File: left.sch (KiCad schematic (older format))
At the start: 87 parts, among them J1 Buzzer_magnetic, J11 Conn_01x01, J12 Conn_01x01, J13 Conn_01x01, J14 Conn_01x01, J15 Conn_01x01, J16 Conn_01x01, J17 Conn_01x01, J2 reset, J25 Buzzer_piezo, J3 ISP, J7 Conn_01x01, J9 UTC16-G, P3 WS2812, P4 SJ-43514-SMT, SW1 Socket, SW10 Socket, SW11 Socket, SW12 Socket, SW13 Socket, SW14 Socket, SW15 Socket, SW16 Socket, SW17 Socket, SW18 Socket, SW19 Socket, SW2 Socket, SW20 Socket, SW21 Socket, SW22 Socket, SW23 Socket, SW24 Socket, SW3 Socket, SW4 Socket, SW49 FSMSM, SW5 Socket, SW6 Socket, SW7 Socket, SW8 Socket, SW9 Socket, U1 ATMega32U4, Y1 16MHz

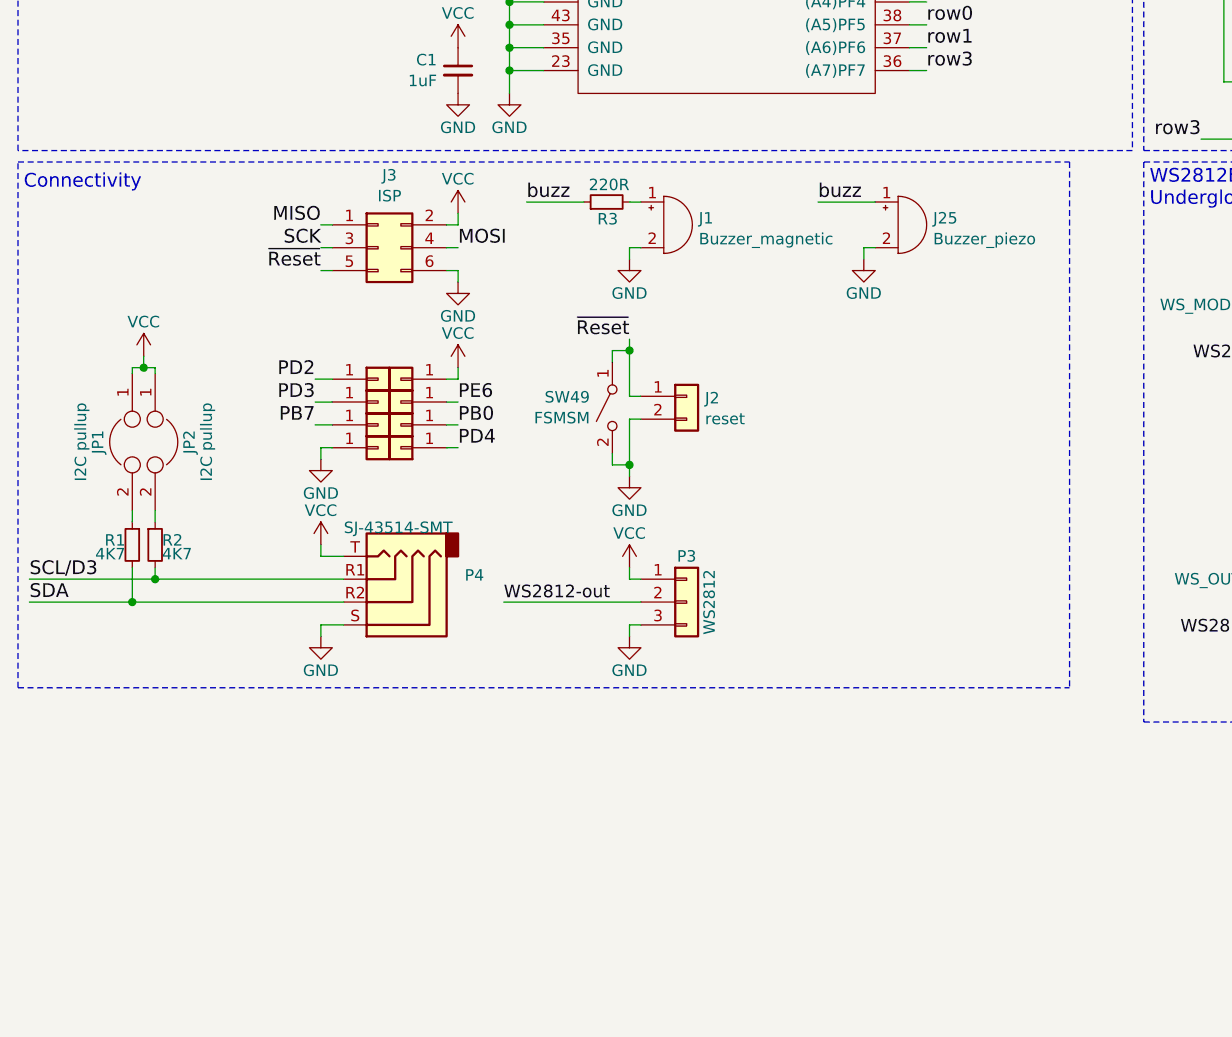
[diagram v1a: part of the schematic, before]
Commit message: Added ESD protection to connectors
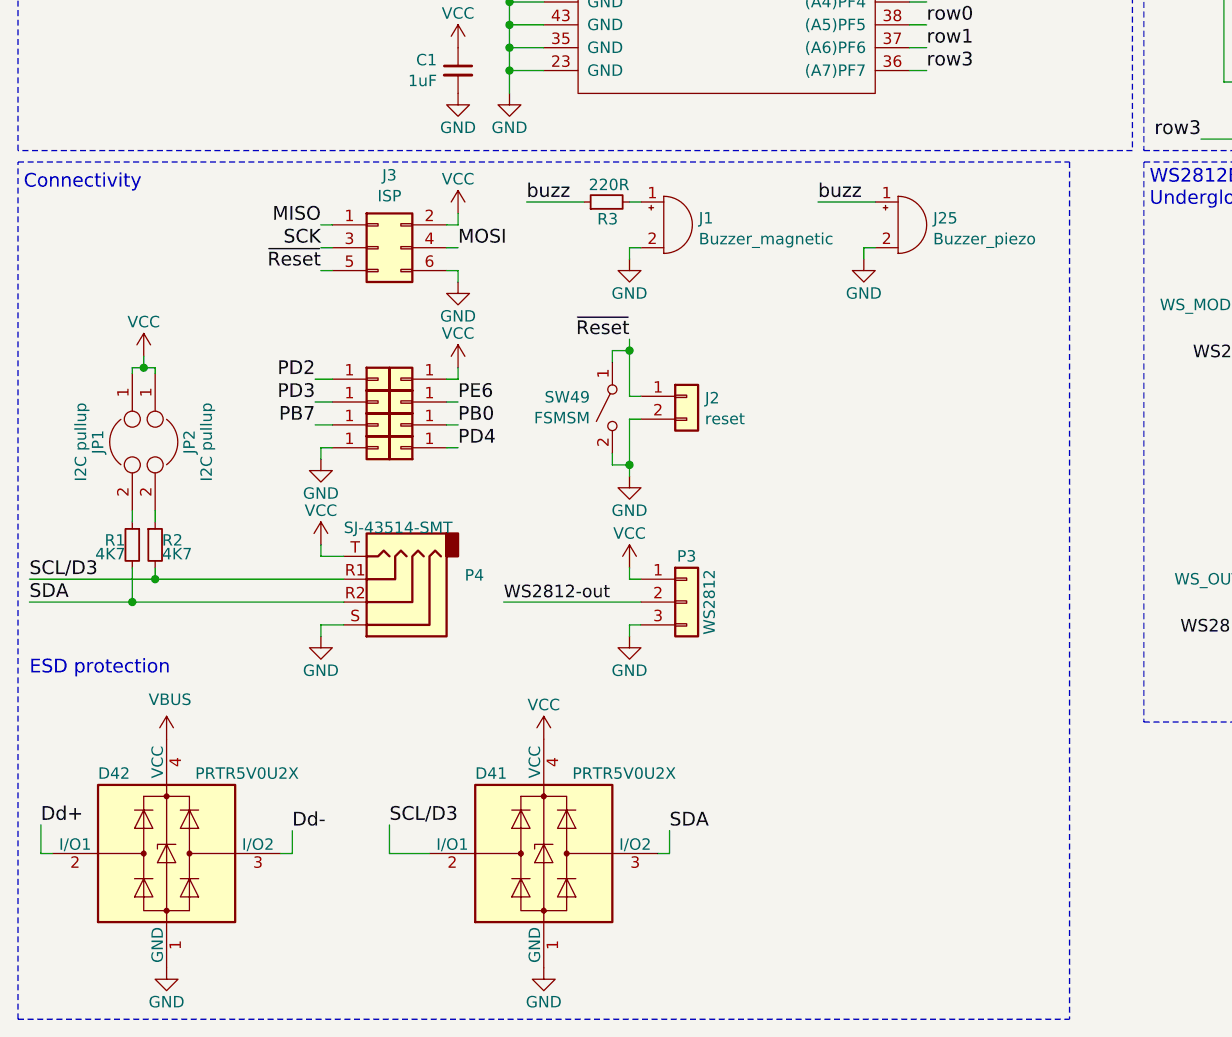
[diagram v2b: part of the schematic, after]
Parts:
- added D41, D42: PRTR5V0U2X, Package_TO_SOT_SMD:SOT-143, symbol Power_Protection:PRTR5V0U2X
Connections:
- net Dd+: now also D42.2 (I/O1)
- net Dd-: now also D42.3 (I/O2)
- net GND: now also D41.1 (GND), D42.1 (GND)
- net SCL/D3: now also D41.2 (I/O1)
- net SDA: now also D41.3 (I/O2)
- net VBUS: now also D42.4 (VCC)
- net VCC: now also D41.4 (VCC)
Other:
- note added: "ESD protection"
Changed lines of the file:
@@
 	875  5925 1325 5925
 Wire Notes Line
-	825  6300 825  4000
+	825  7750 825  4000
 Wire Notes Line
 	825  4000 5425 4000
 Wire Notes Line
-	5425 4000 5425 6300
+	5425 4000 5425 7750
 Wire Notes Line
-	825  6300 5425 6300
+	825  7750 5425 7750
 Text Notes 850  4125 0    60   ~ 0
 Connectivity
@@
 Wire Wire Line
 	4725 2850 4800 2850
+$Comp
+L Power_Protection:PRTR5V0U2X D42
+U 1 1 5D9D619E
+P 1475 7025
+F 0 "D42" H 1175 7375 50  0000 L CNN
+F 1 "PRTR5V0U2X" H 1600 7375 50  0000 L CNN
+F 2 "Package_TO_SOT_SMD:SOT-143" H 1535 7025 50  0001 C CNN
+F 3 "https://assets.nexperia.com/documents/data-sheet/PRTR5V0U2X.pdf" H 1535 7025 50  0001 C CNN
+	1    1475 7025
+	1    0    0    -1
+$EndComp
+$Comp
+L power:VBUS #PWR0131
+U 1 1 5DA6A0DF
+P 1475 6525
+F 0 "#PWR0131" H 1475 6375 50  0001 C CNN
+F 1 "VBUS" H 1490 6698 50  0000 C CNN
+F 2 "" H 1475 6525 50  0001 C CNN
+F 3 "" H 1475 6525 50  0001 C CNN
+	1    1475 6525
+	1    0    0    -1
+$EndComp
+$Comp
+L power:GND #PWR0132
+U 1 1 5DA6AF0C
+P 1475 7525
+F 0 "#PWR0132" H 1475 7275 50  0001 C CNN
+F 1 "GND" H 1475 7375 50  0000 C CNN
+F 2 "" H 1475 7525 50  0000 C CNN
+F 3 "" H 1475 7525 50  0000 C CNN
+	1    1475 7525
+	-1   0    0    -1
+$EndComp
+Wire Wire Line
+	975  7025 925  7025
+Wire Wire Line
+	925  7025 925  6900
+Wire Wire Line
+	1975 7025 2025 7025
+Wire Wire Line
+	2025 7025 2025 6925
+Text Label 925  6900 0    60   ~ 0
+Dd+
+Text Label 2025 6925 0    60   ~ 0
+Dd-
+Text Notes 875  6250 0    60   ~ 0
+ESD protection
+$Comp
+L Power_Protection:PRTR5V0U2X D41
+U 1 1 5DDB696C
+P 3125 7025
+F 0 "D41" H 2825 7375 50  0000 L CNN
+F 1 "PRTR5V0U2X" H 3250 7375 50  0000 L CNN
+F 2 "Package_TO_SOT_SMD:SOT-143" H 3185 7025 50  0001 C CNN
+F 3 "https://assets.nexperia.com/documents/data-sheet/PRTR5V0U2X.pdf" H 3185 7025 50  0001 C CNN
+	1    3125 7025
+	1    0    0    -1
+$EndComp
+$Comp
+L power:GND #PWR0136
+U 1 1 5DDB6980
+P 3125 7525
+F 0 "#PWR0136" H 3125 7275 50  0001 C CNN
+F 1 "GND" H 3125 7375 50  0000 C CNN
+F 2 "" H 3125 7525 50  0000 C CNN
+F 3 "" H 3125 7525 50  0000 C CNN
+	1    3125 7525
+	-1   0    0    -1
+$EndComp
+Wire Wire Line
+	3625 7025 3675 7025
+Wire Wire Line
+	3675 7025 3675 6925
+Text Label 3675 6925 0    60   ~ 0
+SDA
+Text Label 2450 6900 0    60   ~ 0
+SCL/D3
+Wire Wire Line
+	2450 7025 2450 6900
+Wire Wire Line
+	2450 7025 2625 7025
+$Comp
+L power:VCC #PWR0135
+U 1 1 5DF1EEC0
+P 3125 6525
+F 0 "#PWR0135" H 3125 6375 50  0001 C CNN
+F 1 "VCC" H 3125 6675 50  0000 C CNN
+F 2 "" H 3125 6525 50  0000 C CNN
+F 3 "" H 3125 6525 50  0000 C CNN
+	1    3125 6525
+	1    0    0    -1
+$EndComp
 $EndSCHEMATC

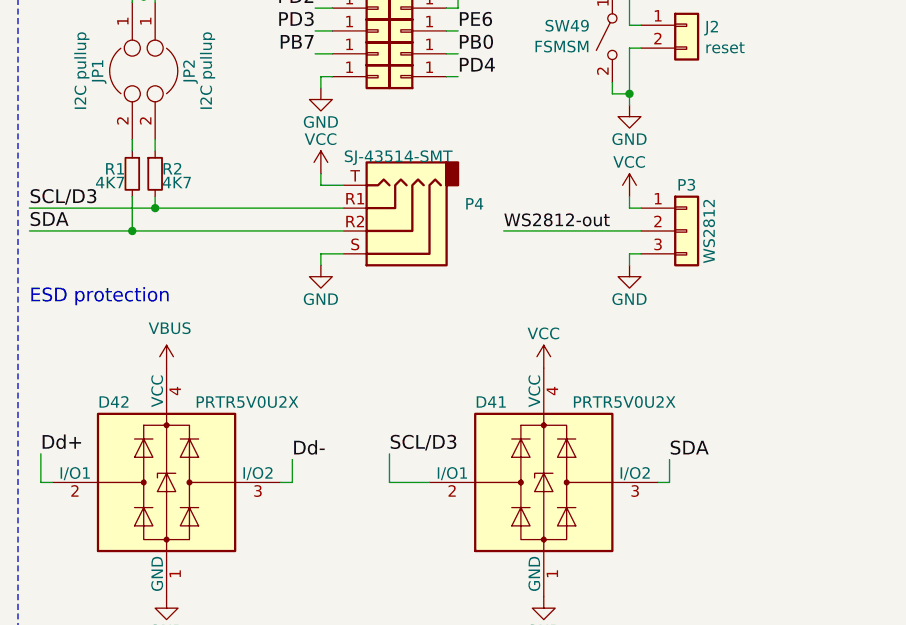
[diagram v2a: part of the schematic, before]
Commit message: Added series resistors on TRRS
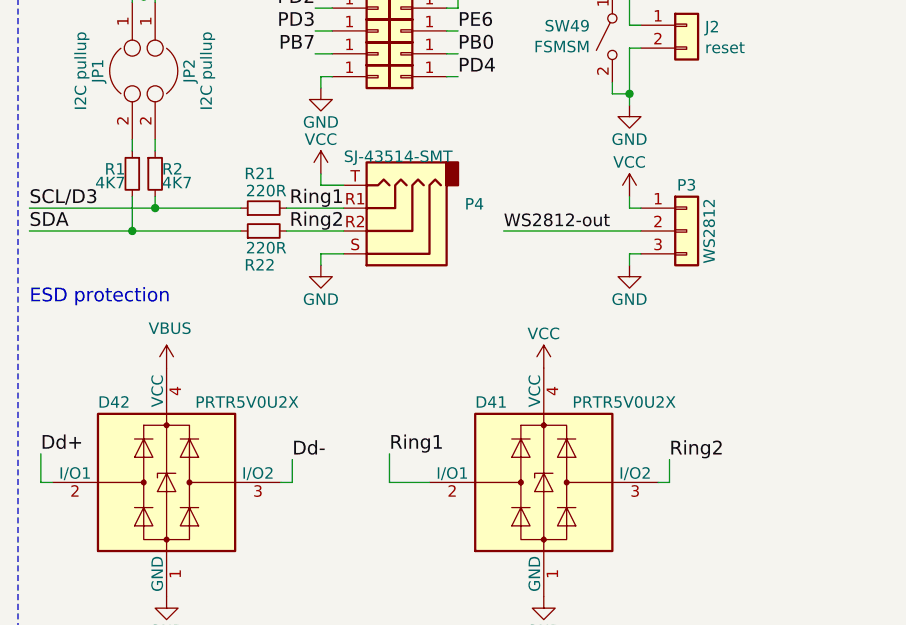
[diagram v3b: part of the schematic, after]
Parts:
- added R21, R22: 220R, Resistor_SMD:R_0603_1608Metric, symbol Device:R_Small
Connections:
- net SCL/D3: now also R21.1; no longer D41.2 (I/O1), P4.R1
- net SDA: now also R22.1; no longer D41.3 (I/O2), P4.R2
- new net Ring1: D41.2 (I/O1), P4.R1, R21.2
- new net Ring2: D41.3 (I/O2), P4.R2, R22.2
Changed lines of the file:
@@
 Wire Wire Line
 	2150 6075 2150 6025
-Connection ~ 1325 5925
 Wire Wire Line
 	1425 5525 1425 5575
@@
 Wire Wire Line
 	875  5825 1425 5825
-Connection ~ 1425 5825
-Wire Wire Line
-	1425 5825 2250 5825
-Wire Wire Line
-	1325 5925 2250 5925
 Wire Wire Line
 	875  5925 1325 5925
@@
 Wire Wire Line
 	3675 7025 3675 6925
-Text Label 3675 6925 0    60   ~ 0
-SDA
-Text Label 2450 6900 0    60   ~ 0
-SCL/D3
 Wire Wire Line
 	2450 7025 2450 6900
@@
 	1    0    0    -1
 $EndComp
+Connection ~ 1425 5825
+Connection ~ 1325 5925
+Wire Wire Line
+	2000 5825 2250 5825
+Wire Wire Line
+	2250 5925 2000 5925
+Wire Wire Line
+	1800 5925 1325 5925
+Wire Wire Line
+	1800 5825 1425 5825
+$Comp
+L Device:R_Small R21
+U 1 1 5D9D64B4
+P 1900 5825
+F 0 "R21" V 2050 5775 50  0000 L CNN
+F 1 "220R" V 1975 5725 50  0000 L CNN
+F 2 "Resistor_SMD:R_0603_1608Metric" H 1900 5825 50  0001 C CNN
+F 3 "" H 1900 5825 50  0000 C CNN
+	1    1900 5825
+	0    -1   -1   0
+$EndComp
+$Comp
+L Device:R_Small R22
+U 1 1 5DA3BD0C
+P 1900 5925
+F 0 "R22" V 1750 5875 50  0000 L CNN
+F 1 "220R" V 1825 5825 50  0000 L CNN
+F 2 "Resistor_SMD:R_0603_1608Metric" H 1900 5925 50  0001 C CNN
+F 3 "" H 1900 5925 50  0000 C CNN
+	1    1900 5925
+	0    -1   -1   0
+$EndComp
+Text Label 2250 5825 2    60   ~ 0
+Ring1
+Text Label 2250 5925 2    60   ~ 0
+Ring2
+Text Label 2450 6900 0    60   ~ 0
+Ring1
+Text Label 3675 6925 0    60   ~ 0
+Ring2
 $EndSCHEMATC

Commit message: Added PE2 pull-down for dfu
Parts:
- added R?: 100k, Resistor_SMD:R_0603_1608Metric, symbol Device:R_Small
- U1: symbol 8Bit-MCU:ATMega32U4 -> vitamins_included-rescue:ATMega32U4-8Bit-MCU
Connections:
- net GND: now also R?.1
- net col2: now also R?.2
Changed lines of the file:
@@
 EESchema Schematic File Version 4
-LIBS:vitamins_included-cache
-EELAYER 29 0
+EELAYER 30 0
 EELAYER END
 $Descr A4 11693 8268
@@
 $EndComp
 $Comp
-L 8Bit-MCU:ATMega32U4 U1
+L vitamins_included-rescue:ATMega32U4-8Bit-MCU U1
 U 1 1 5A0C4D11
 P 3375 1550
@@
 Wire Wire Line
 	5475 2500 5600 2500
-Wire Wire Line
-	5600 2500 5600 2550
 $Comp
 L power:GND #PWR0101
 U 1 1 5B621855
-P 5600 2550
-F 0 "#PWR0101" H 5600 2300 50  0001 C CNN
-F 1 "GND" H 5600 2400 50  0000 C CNN
-F 2 "" H 5600 2550 50  0000 C CNN
-F 3 "" H 5600 2550 50  0000 C CNN
-	1    5600 2550
+P 5600 2900
+F 0 "#PWR0101" H 5600 2650 50  0001 C CNN
+F 1 "GND" H 5600 2750 50  0000 C CNN
+F 2 "" H 5600 2900 50  0000 C CNN
+F 3 "" H 5600 2900 50  0000 C CNN
+	1    5600 2900
 	1    0    0    -1
 $EndComp
@@
 Text Label 4800 2850 0    60   ~ 0
 col2
-Wire Wire Line
-	4725 2850 4800 2850
 $Comp
 L Power_Protection:PRTR5V0U2X D42
@@
 Text Label 3675 6925 0    60   ~ 0
 Ring2
+$Comp
+L Device:R_Small R?
+U 1 1 5F759A1C
+P 5375 2850
+F 0 "R?" V 5525 2775 50  0000 L CNN
+F 1 "100k" V 5450 2750 50  0000 L CNN
+F 2 "Resistor_SMD:R_0603_1608Metric" H 5375 2850 50  0001 C CNN
+F 3 "" H 5375 2850 50  0000 C CNN
+	1    5375 2850
+	0    1    1    0
+$EndComp
+Wire Wire Line
+	4725 2850 5275 2850
+Wire Wire Line
+	5600 2900 5600 2850
+Wire Wire Line
+	5600 2850 5475 2850
+Wire Wire Line
+	5600 2500 5600 2850
+Connection ~ 5600 2850
 $EndSCHEMATC

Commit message: saved schematics
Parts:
- gave numbers to parts that had none: 1
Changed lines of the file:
@@
 Ring2
 $Comp
-L Device:R_Small R?
+L Device:R_Small R25
 U 1 1 5F759A1C
 P 5375 2850
-F 0 "R?" V 5525 2775 50  0000 L CNN
+F 0 "R25" V 5525 2775 50  0000 L CNN
 F 1 "100k" V 5450 2750 50  0000 L CNN
 F 2 "Resistor_SMD:R_0603_1608Metric" H 5375 2850 50  0001 C CNN
